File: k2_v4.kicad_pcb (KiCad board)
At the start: 8 copper layers, 120 x 38 mm, 101 parts, among them J11 J_EC_HEADER, J12 J_12V_IN, J13 J_SWD, J2 SlimSAS_x8_SFF8654, J3 MCIO_4i_SFF1016, J4 MCIO_4i_SFF1016, J6 J_PWR_CTRL, J9 J_OOB_HEADER, U1 STM32G0B1CBT6, U2 DCDC_12V_3V3, U3 DS160PR810, U4 BAT54C, U5 OPTO_LTV356T, U7 DS160PR810

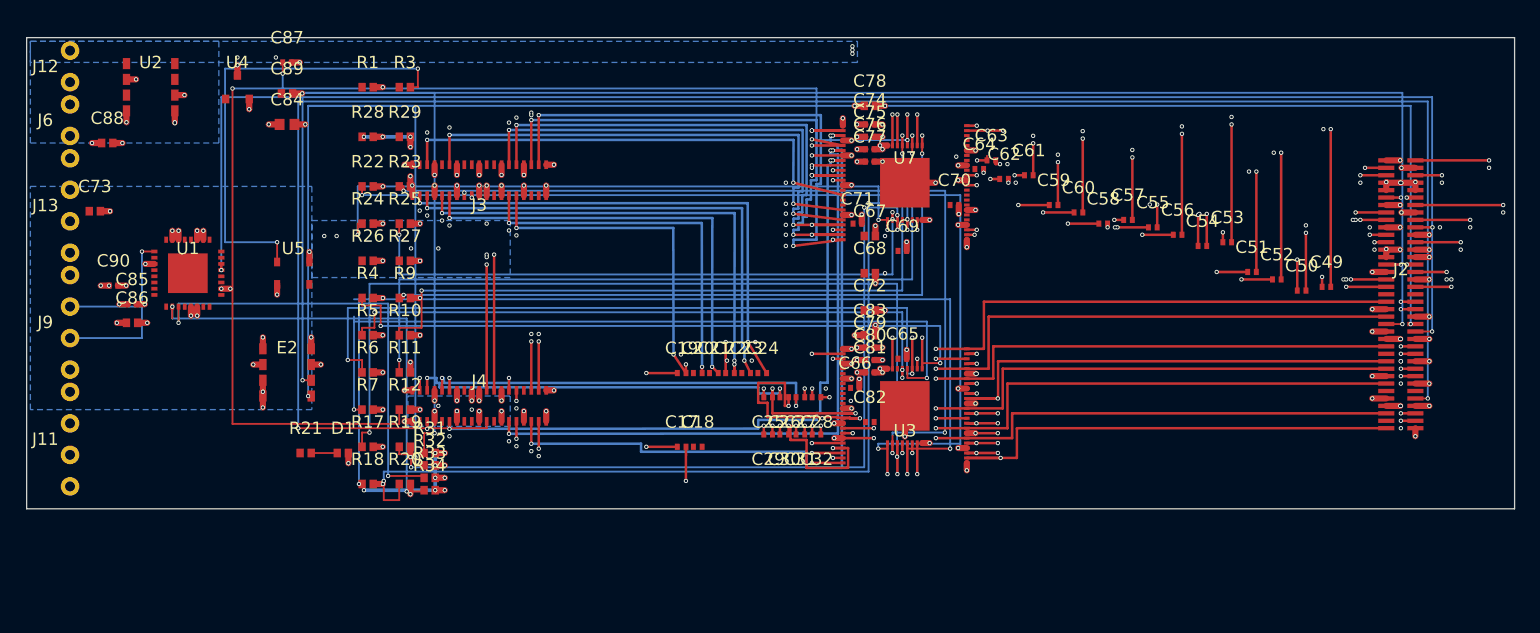
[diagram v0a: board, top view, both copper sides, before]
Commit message: feat(k2): M13 卡0.5 权威生成器迁移 + 复摆落位 — k2_gen_v5 迁 k2/tools/ + uuid5 确定性化(零运行时自由度) + k2_sch.yaml 补 C88/C89(card=2) + 电容墙复摆落位(k2_v4 87b66fbb→6c387dff, 32/32 at 与 solve_v2 逐字节一致) + submodule 指针 e4637e0→5643a21
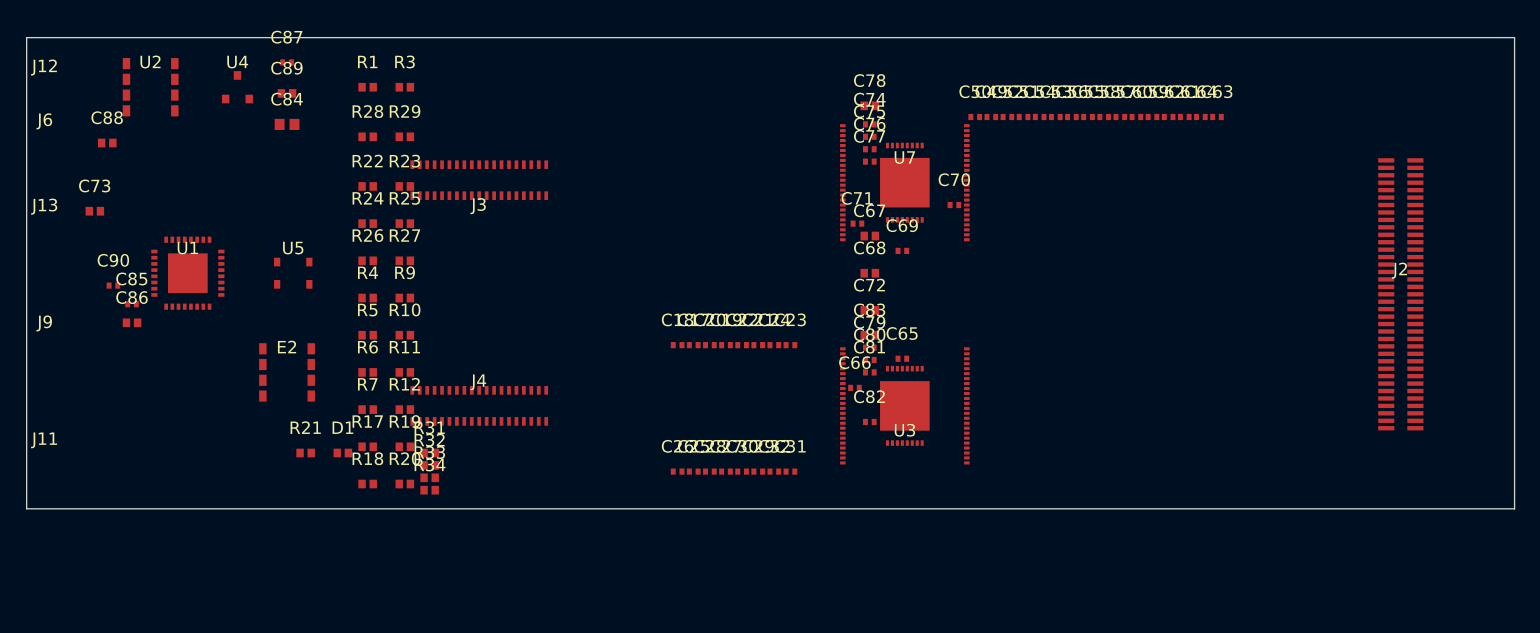
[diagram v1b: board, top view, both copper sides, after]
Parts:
- moved C49 30.3 mm to (100.8, 39.4)
- moved C50 29.8 mm to (99.5, 39.4)
- moved C52 25.4 mm to (102.1, 39.4)
- moved C51 22.3 mm to (103.4, 39.4)
- moved C63 18.5 mm to (119.0, 39.4)
- moved C64 18.4 mm to (117.7, 39.4)
- moved C53 17.1 mm to (106.0, 39.4)
- moved C54 16.7 mm to (104.7, 39.4)
- moved C62 14.2 mm to (115.1, 39.4)
- moved C61 13.4 mm to (116.4, 39.4)
- moved C56 12.8 mm to (107.3, 39.4)
- moved C59 10.7 mm to (113.8, 39.4)
- moved C28 10.5 mm to (78.1, 68.0), turned to 0 degrees
- moved C26 10.5 mm to (75.5, 68.0), turned to 0 degrees
- moved C55 10.3 mm to (108.6, 39.4)
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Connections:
- U1 pad 18: NO_CONNECT -> GND
- U1 pad 21: NO_CONNECT -> GND
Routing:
- net I2C1_SCL: track 173.1 -> 0.00 mm, vias 3 -> 0
- net I2C1_SDA: track 168.9 -> 0.00 mm, vias 3 -> 0
- net PERSTB#: track 158.1 -> 0.00 mm, vias 2 -> 0
- net PERSTA#: track 135.7 -> 0.00 mm, vias 3 -> 0
- net GND: track 109.8 -> 0.00 mm, vias 198 -> 0
- net STRAP_EQ1_U7: track 103.2 -> 0.00 mm, vias 3 -> 0
- net PCIE_REFCLK1_N: track 86.0 -> 0.00 mm, vias 2 -> 0
- net PCIE_REFCLK1_P: track 85.1 -> 0.00 mm, vias 2 -> 0
- net PD0_U3: track 80.1 -> 0.00 mm, vias 3 -> 0
- net STRAP_EQ1_1_U3: track 80.1 -> 0.00 mm, vias 3 -> 0
- net PCIE_REFCLK0_N: track 77.3 -> 0.00 mm, vias 2 -> 0
- net PCIE_REFCLK0_P: track 76.3 -> 0.00 mm, vias 2 -> 0
- net STRAP_EQ0_1_U3: track 73.8 -> 0.00 mm, vias 3 -> 0
- net PCIE_UP7_N: track 72.9 -> 0.00 mm, vias 3 -> 0
- net PCIE_UP6_N: track 71.2 -> 0.00 mm, vias 3 -> 0
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- removed copper zone on In1.Cu, net GND
- removed copper zone on In3.Cu, net GND
- removed copper zone on In5.Cu, net GND
- removed copper zone on In4.Cu, net MCU_VDD
- removed copper zone on B.Cu, net P3V3
- removed copper zone on In4.Cu, net P3V3
- removed copper zone on B.Cu, net P3V3_AUX

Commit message: docs(k2): M14 v30 scope-B 真板物理 ECO + A/B 端口对账修正 (用户/架构裁决)
裁决门: TI 三重主源 (SNLS683 T5-1 + SNLA425 T1-2/1-3 + SNLU300 2.4) 证明 A/B 前缀=方向通道组
(非空间端口组): host(J2)端球=A_PER+B_PET, device(MCIO)端球=A_PET+B_PER -> 对账修正 A_PET<->B_PET
换位 (L1/L2 v2.0 补记 + C5 矩阵 _v30_scopeB_correction), 6L 判定不变未触发 8L 重入.

真板物理 ECO (pcbnew, 备份 .bak_scopeB_v29 sha 6c387dff): 删 60 件旧 DS160PR810 域 (U3/U7 +
AC墙 C17-32+C49-64 + VREG C65-72 + 旧strap R4-27) + 插 DS320PR1601 U6 @(93.8,53.7) rot90(A1->SW,
裁决 rot-270 语义的 KiCad 实际角) + 64 信号球按修正 C5 矩阵接线 (A_PER->PCIE_DN*, B_PET->
UP_OUT*_J2, A_PET->DN_OUT*_MCIO, B_PER->UP*) + VCC30->P3V3 + GND152 + 板框 y33->79(46mm) +
8L->6L. C5 芯片级实测 130 断言 PASS (含 REFCLK 直通断言, 旧网零残留).

open gaps 如实登记: DS320 侧带 17 球无冻结设计意图 / C79+C83 去耦落 DS320 球域 / SPEC
port_to_corridor 带前缀键无法表达修正后逐带映射(ECN 候选) / sch 侧仍 U3/U7 / L3 施工验证未启动
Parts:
- removed C17, C18, C19, C20, C21, C22, C23, C24, C25, C26, C27, C28, C29, C30, C31, C32, C49, C50, C51, C52, C53, C54, C55, C56, C57, C58, C59, C60, C61, C62, C63, C64: 220nF, Capacitor_SMD:C_0402_1005Metric
- removed C65, C66, C69, C70, C71: 100nF, Capacitor_SMD:C_0402_1005Metric
- removed C67, C68, C72: 100nF, Capacitor_SMD:C_0603_1608Metric
- removed R10, R22, R23, R24, R25, R5: 1K, Resistor_SMD:R_0603_1608Metric
- removed R11, R17, R19, R6: 13K, Resistor_SMD:R_0603_1608Metric
- removed R12, R18, R20, R7: 59K, Resistor_SMD:R_0603_1608Metric
- removed R26, R27: 4.7k, Resistor_SMD:R_0603_1608Metric
- removed R4, R9: 10K, Resistor_SMD:R_0603_1608Metric
- removed U3, U7: DS160PR810, ForgeOS:WQFN-64_10x5.5mm_P0.4mm
- added U6: DS320PR1601, DS320PR1601, F.Cu at (93.8, 53.7)
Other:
- board size 120 x 38 mm -> 120 x 46 mm
- copper layers 8 -> 6
